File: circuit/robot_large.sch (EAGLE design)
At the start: 15 parts, among them M1 SERVO-FLIPPED, M2 SERVO-1, M3 SERVO-1, U1 ESP01

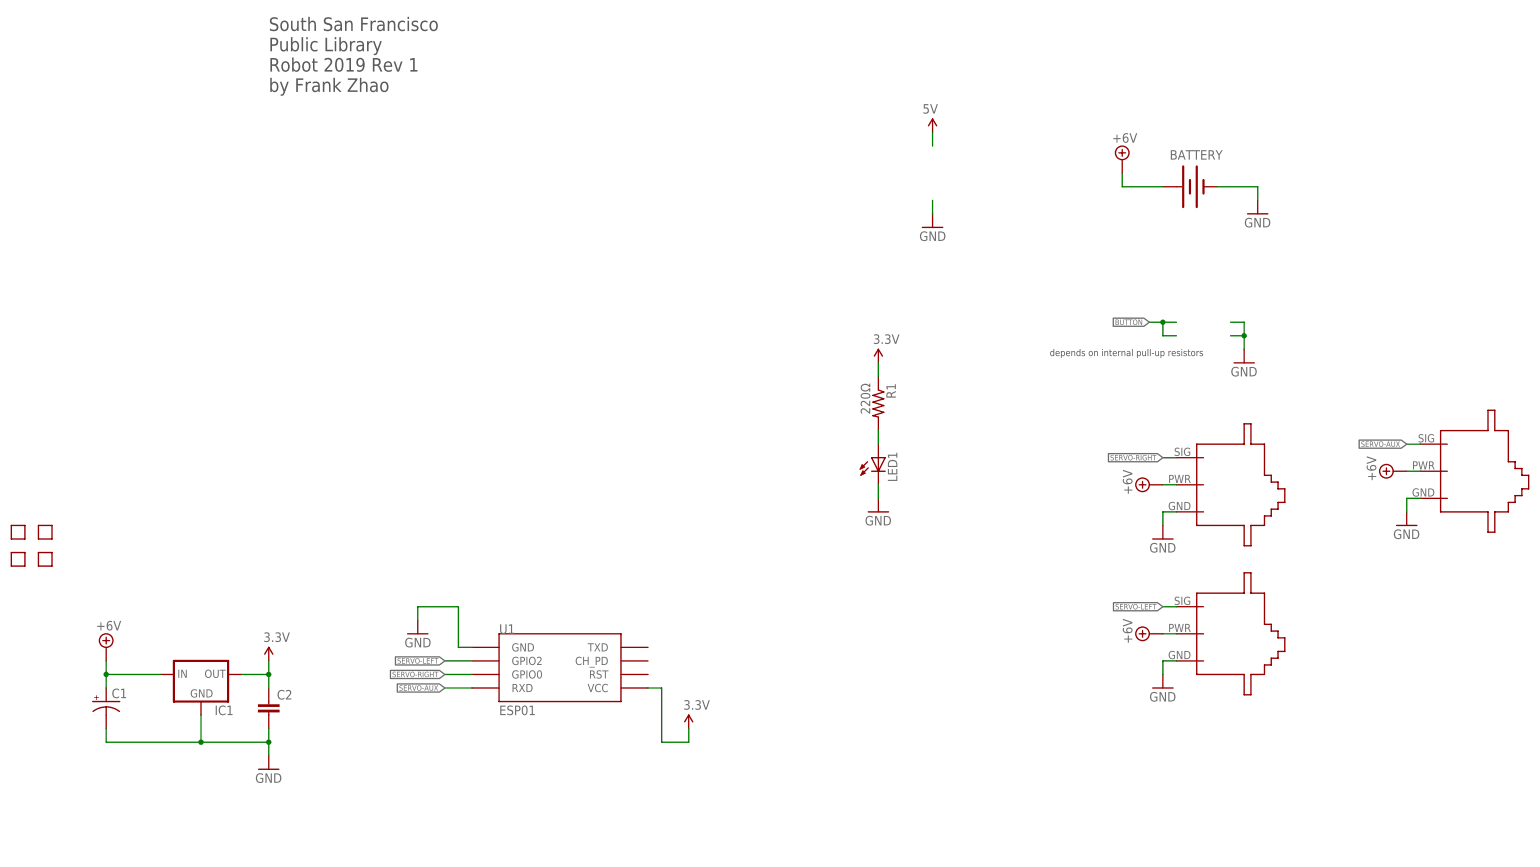
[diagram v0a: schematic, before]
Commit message: smaller pcb
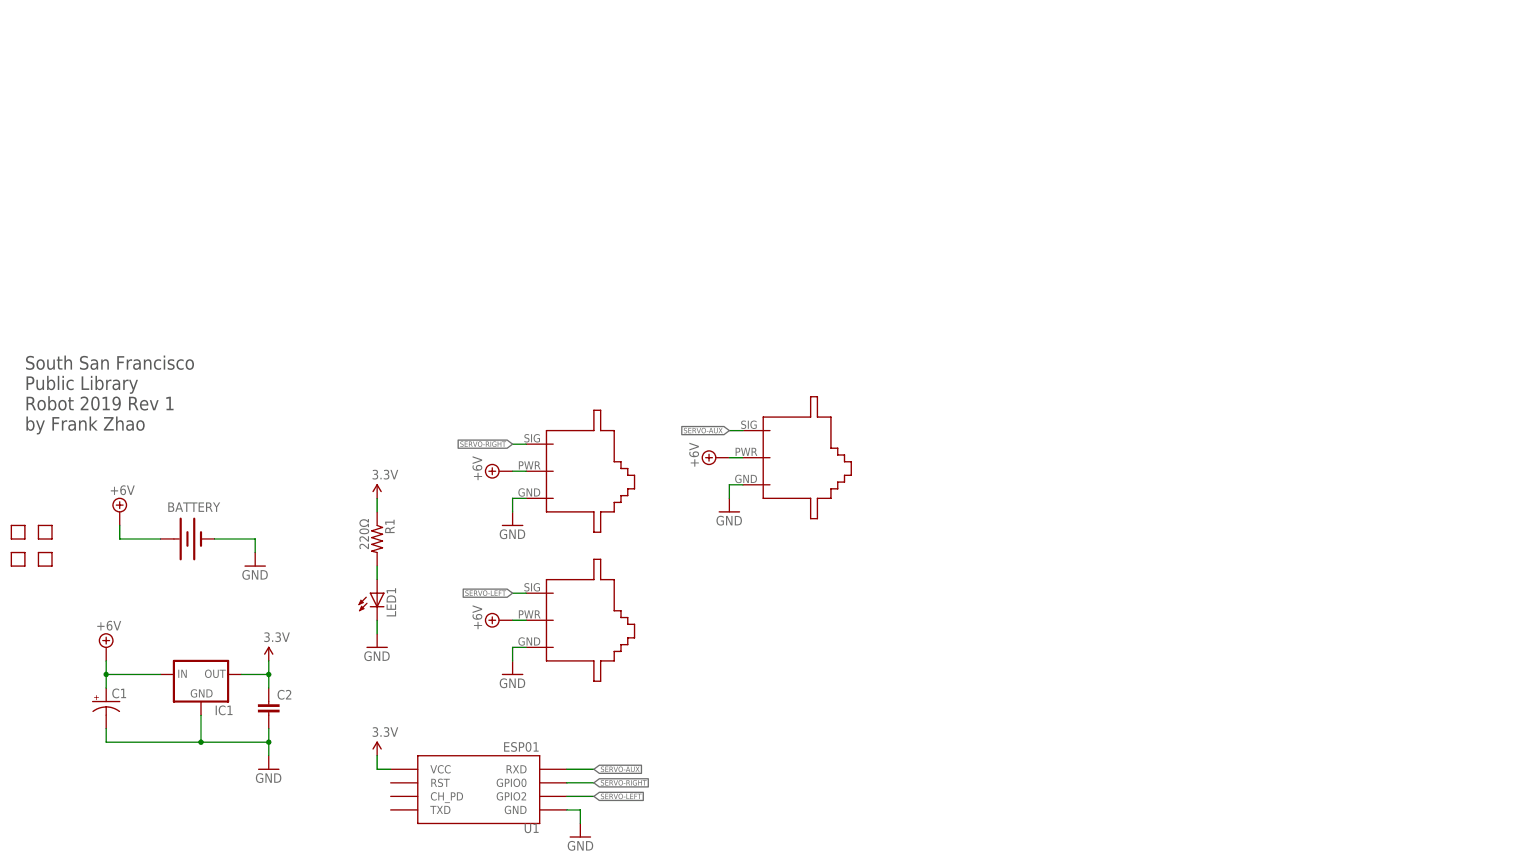
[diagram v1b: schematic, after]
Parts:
- R1: device robot:RESISTORAXIAL-0.3 -> robot:RESISTORAXIAL-0.3-NOVAL
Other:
- note removed: "depends on internal pull-up resistors"
- moved on the sheet: BATTERY, LED1, R1, U1
